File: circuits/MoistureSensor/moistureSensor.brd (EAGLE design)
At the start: 30.1 x 19 mm, 8 parts, among them P1 MCS10B, P2 MCS10B, Q1 BSS84

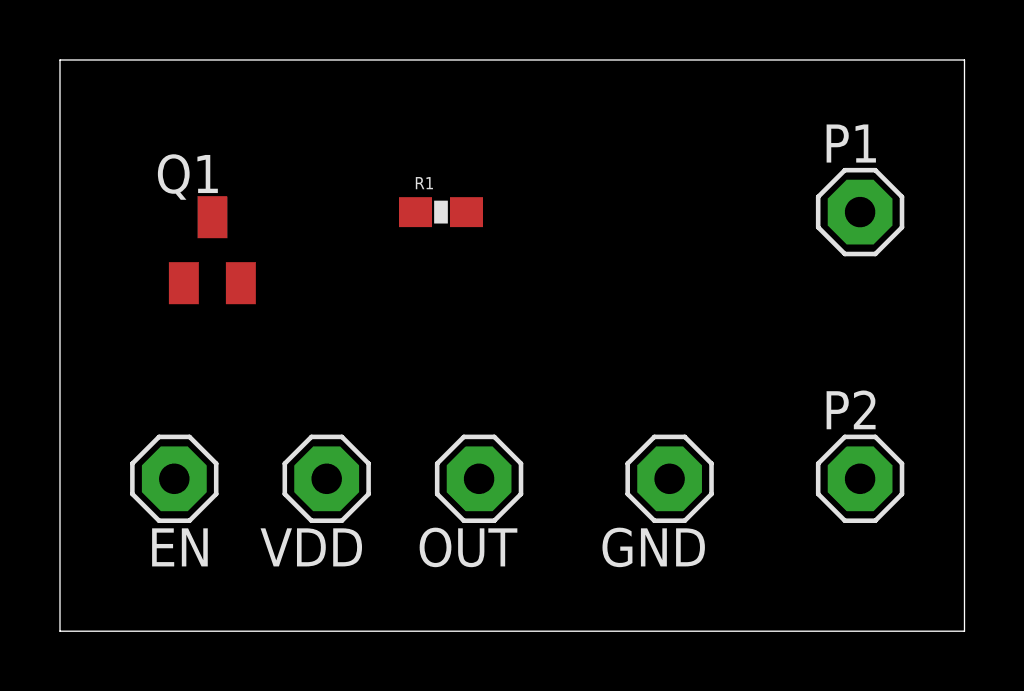
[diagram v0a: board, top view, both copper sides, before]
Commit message: Swapped probe and resistor positions
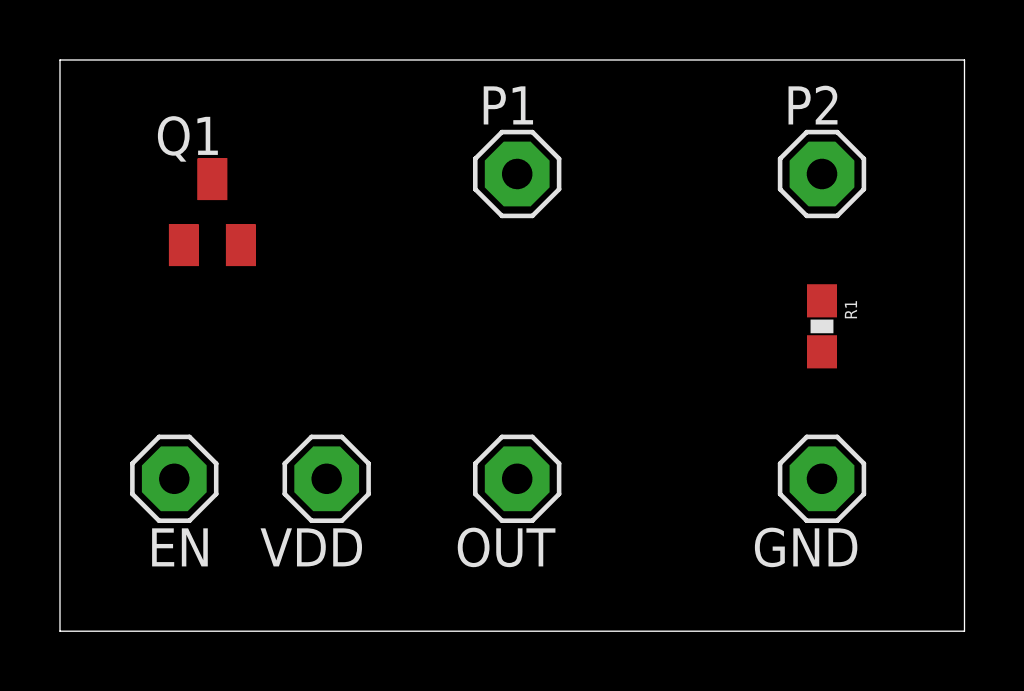
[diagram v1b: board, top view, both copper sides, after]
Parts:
- moved R1 13.3 mm to (21.6, 50.8), turned to 270 degrees
- moved P1 11.5 mm to (11.4, 55.9)
- moved P2 10.2 mm to (21.6, 55.9)
- moved GND 5.08 mm to (21.6, 45.7)
- moved OUT 1.27 mm to (11.4, 45.7)
- moved Q1 1.27 mm to (1.27, 54.6)
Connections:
- net GND: now also R1.2; no longer P2.MP
- net N$1: now also P2.MP; no longer Q1.3
- net N$3: now also Q1.3; no longer R1.2
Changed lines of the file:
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@@
 </autorouter>
 <elements>
-<element name="Q1" library="transistor-small-signal" package="SOT23" value="BSS84" x="1.27" y="53.34"/>
-<element name="R1" library="SparkFun-Resistors" package="0603-RES" value="1M" x="8.89" y="54.61">
-<attribute name="PROD_ID" value="RES-07868" x="8.89" y="54.61" size="1.778" layer="27" display="off"/>
-</element>
-<element name="P1" library="solpad" package="MCS10B" value="MCS10B" x="22.86" y="54.61"/>
-<element name="P2" library="solpad" package="MCS10B" value="MCS10B" x="22.86" y="45.72"/>
-<element name="GND" library="solpad" package="MCS10B" value="MCS10B" x="16.51" y="45.72" rot="R180"/>
+<element name="Q1" library="transistor-small-signal" package="SOT23" value="BSS84" x="1.27" y="54.61"/>
+<element name="P1" library="solpad" package="MCS10B" value="MCS10B" x="11.43" y="55.88"/>
+<element name="P2" library="solpad" package="MCS10B" value="MCS10B" x="21.59" y="55.88"/>
+<element name="GND" library="solpad" package="MCS10B" value="MCS10B" x="21.59" y="45.72" rot="R180"/>
 <element name="VDD" library="solpad" package="MCS10B" value="MCS10B" x="5.08" y="45.72" rot="R180"/>
 <element name="EN" library="solpad" package="MCS10B" value="MCS10B" x="0" y="45.72" rot="R180"/>
-<element name="OUT" library="solpad" package="MCS10B" value="MCS10B" x="10.16" y="45.72" rot="R180"/>
+<element name="OUT" library="solpad" package="MCS10B" value="MCS10B" x="11.43" y="45.72" rot="R180"/>
+<element name="R1" library="SparkFun-Resistors" package="0603-RES" value="1M" x="21.59" y="50.8" rot="R270">
+<attribute name="PROD_ID" value="RES-07868" x="21.59" y="50.8" size="1.778" layer="27" rot="R270" display="off"/>
+</element>
 </elements>
 <signals>
-<signal name="N$1">
-<contactref element="R1" pad="1"/>
-<contactref element="Q1" pad="3"/>
-<wire x1="8.04" y1="54.61" x2="1.27" y2="54.44" width="0" layer="19" extent="1-1"/>
-</signal>
 <signal name="N$3">
-<contactref element="R1" pad="2"/>
 <contactref element="P1" pad="MP"/>
 <contactref element="OUT" pad="MP"/>
-<wire x1="9.74" y1="54.61" x2="22.86" y2="54.61" width="0" layer="19" extent="1-1"/>
-<wire x1="10.16" y1="45.72" x2="9.74" y2="54.61" width="0" layer="19" extent="1-1"/>
+<contactref element="Q1" pad="3"/>
+<wire x1="11.43" y1="45.72" x2="11.43" y2="55.88" width="0" layer="19" extent="1-1"/>
+<wire x1="1.27" y1="55.71" x2="11.43" y2="45.72" width="0" layer="19" extent="1-1"/>
 </signal>
 <signal name="VDD">
 <contactref element="Q1" pad="2"/>
 <contactref element="VDD" pad="MP"/>
-<wire x1="5.08" y1="45.72" x2="2.22" y2="52.24" width="0" layer="19" extent="1-1"/>
+<wire x1="5.08" y1="45.72" x2="2.22" y2="53.51" width="0" layer="19" extent="1-1"/>
 </signal>
 <signal name="GND">
-<contactref element="P2" pad="MP"/>
 <contactref element="GND" pad="MP"/>
-<wire x1="16.51" y1="45.72" x2="22.86" y2="45.72" width="0" layer="19" extent="1-1"/>
+<contactref element="R1" pad="2"/>
+<wire x1="21.59" y1="49.95" x2="21.59" y2="45.72" width="0" layer="19" extent="1-1"/>
 </signal>
 <signal name="N$2">
 <contactref element="EN" pad="MP"/>
 <contactref element="Q1" pad="1"/>
-<wire x1="0" y1="45.72" x2="0.32" y2="52.24" width="0" layer="19" extent="1-1"/>
+<wire x1="0" y1="45.72" x2="0.32" y2="53.51" width="0" layer="19" extent="1-1"/>
+</signal>
+<signal name="N$1">
+<contactref element="P2" pad="MP"/>
+<contactref element="R1" pad="1"/>
+<wire x1="21.59" y1="51.65" x2="21.59" y2="55.88" width="0" layer="19" extent="1-1"/>
 </signal>
 </signals>
